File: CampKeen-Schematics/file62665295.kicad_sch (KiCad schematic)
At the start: 29 parts, among them Q2 2N7000, Q3 IRF9Z34NPBF, Q4 2N7000, Q5 2N7000, Q58 LTV-847, Q6 2N7000, Q7 2N7000

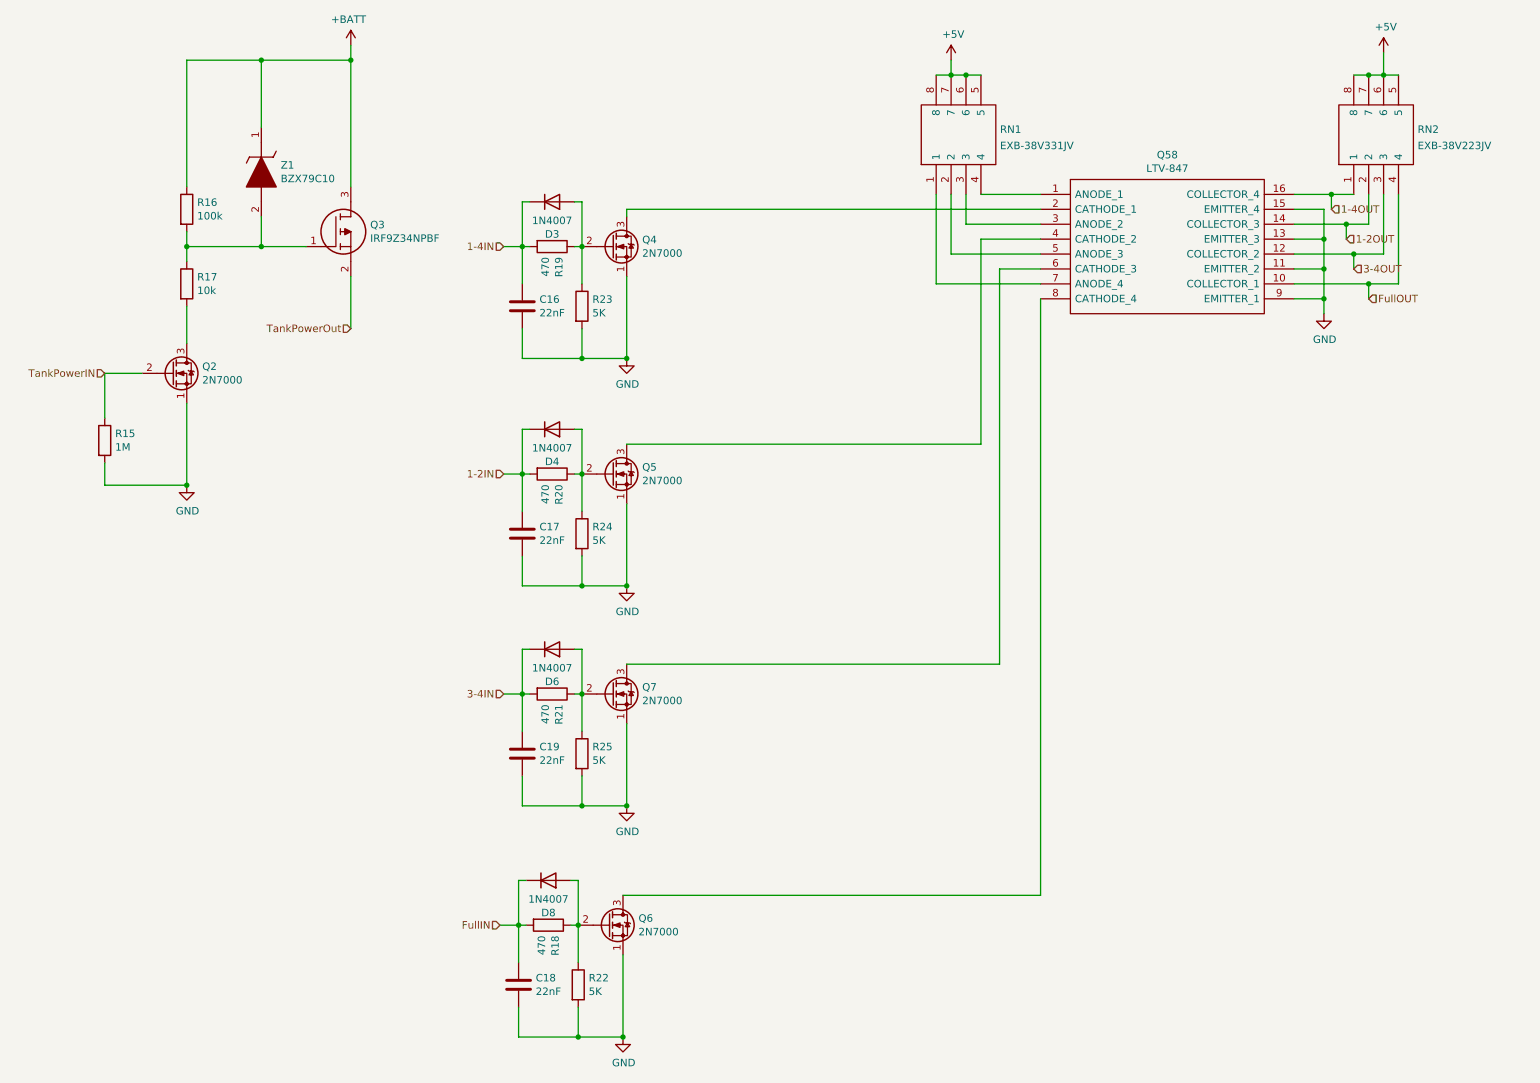
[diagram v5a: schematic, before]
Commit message: working on the input changes. removing all of the inverters. requires a code change. waiting on a part file to add the possible TVS diode
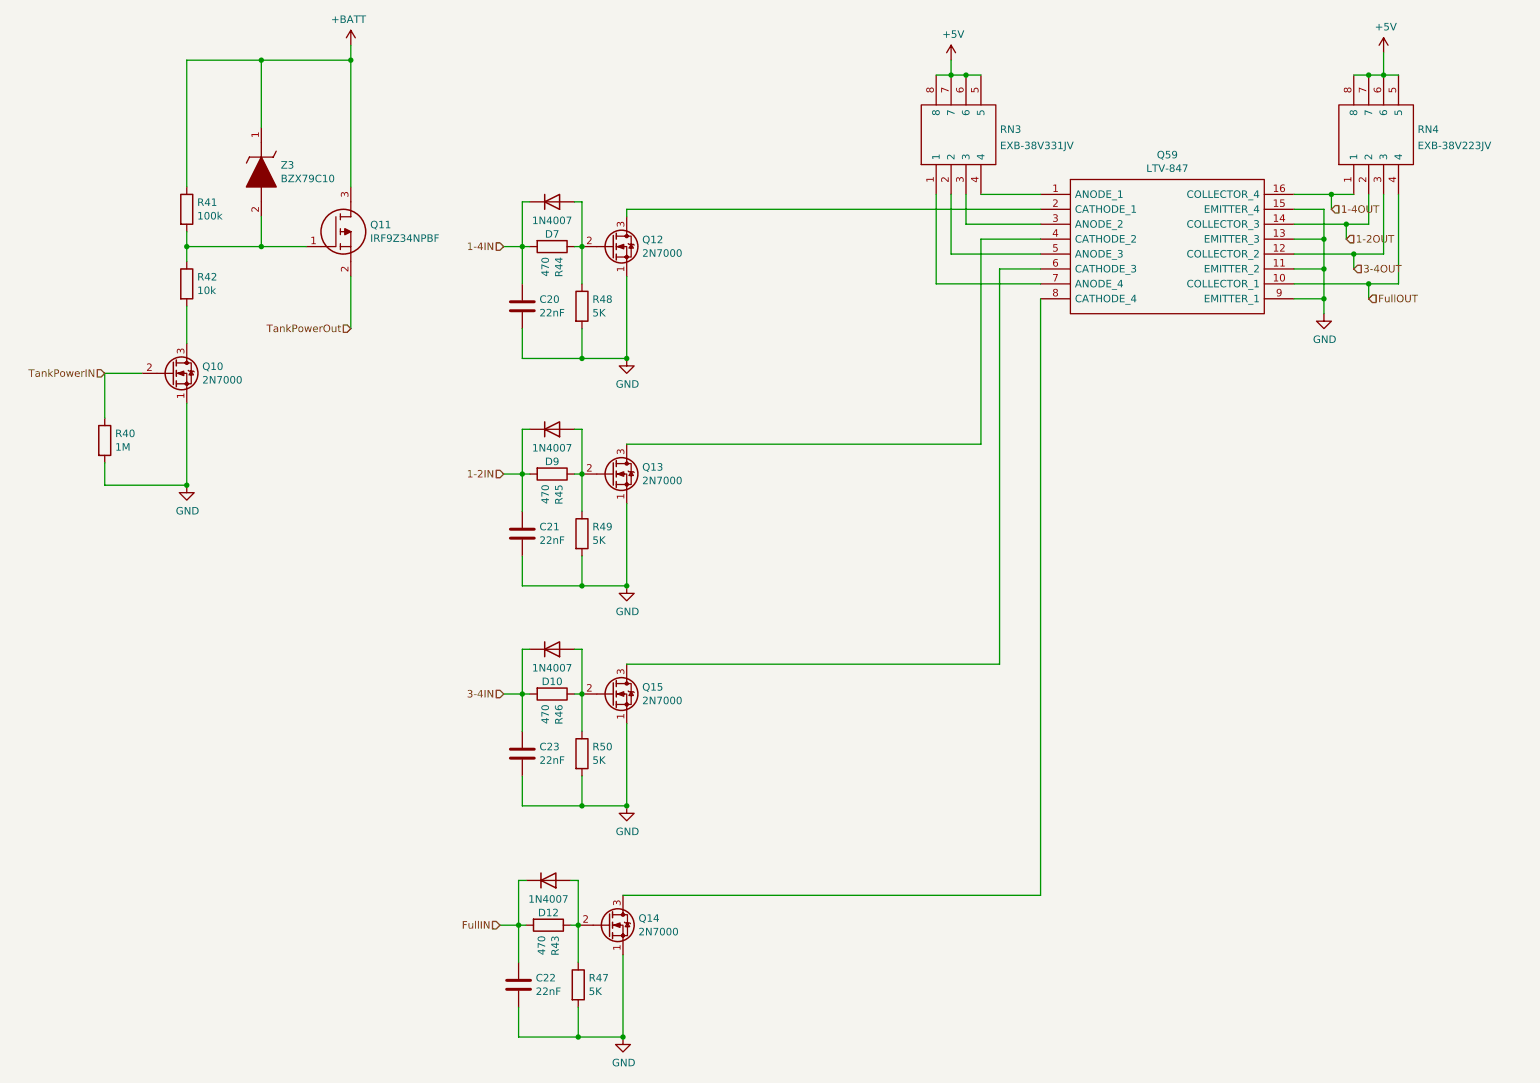
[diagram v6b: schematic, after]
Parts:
- C20: renamed from C16; footprint Capacitor_THT:C_Disc_D4.7mm_W2.5mm_P5.00mm -> Capacitor_SMD:C_0603_1608Metric_Pad1.08x0.95mm_HandSolder
- C21: renamed from C17; footprint Capacitor_THT:C_Disc_D4.7mm_W2.5mm_P5.00mm -> Capacitor_SMD:C_0603_1608Metric_Pad1.08x0.95mm_HandSolder
- C22: renamed from C18; footprint Capacitor_THT:C_Disc_D4.7mm_W2.5mm_P5.00mm -> Capacitor_SMD:C_0603_1608Metric_Pad1.08x0.95mm_HandSolder
- C23: renamed from C19; footprint Capacitor_THT:C_Disc_D4.7mm_W2.5mm_P5.00mm -> Capacitor_SMD:C_0603_1608Metric_Pad1.08x0.95mm_HandSolder
- renumbered D6 to D10, D8 to D12, D3 to D7, D4 to D9, Q2 to Q10, Q3 to Q11, Q4 to Q12, Q5 to Q13, Q6 to Q14, Q7 to Q15, Q58 to Q59, R15 to R40, R16 to R41, R17 to R42, R18 to R43, R19 to R44, R20 to R45, R21 to R46, R22 to R47, R23 to R48, R24 to R49, R25 to R50, RN1 to RN3, RN2 to RN4, Z1 to Z3

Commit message: working on getting the board cleaned enough to start placing the new designs and chips.
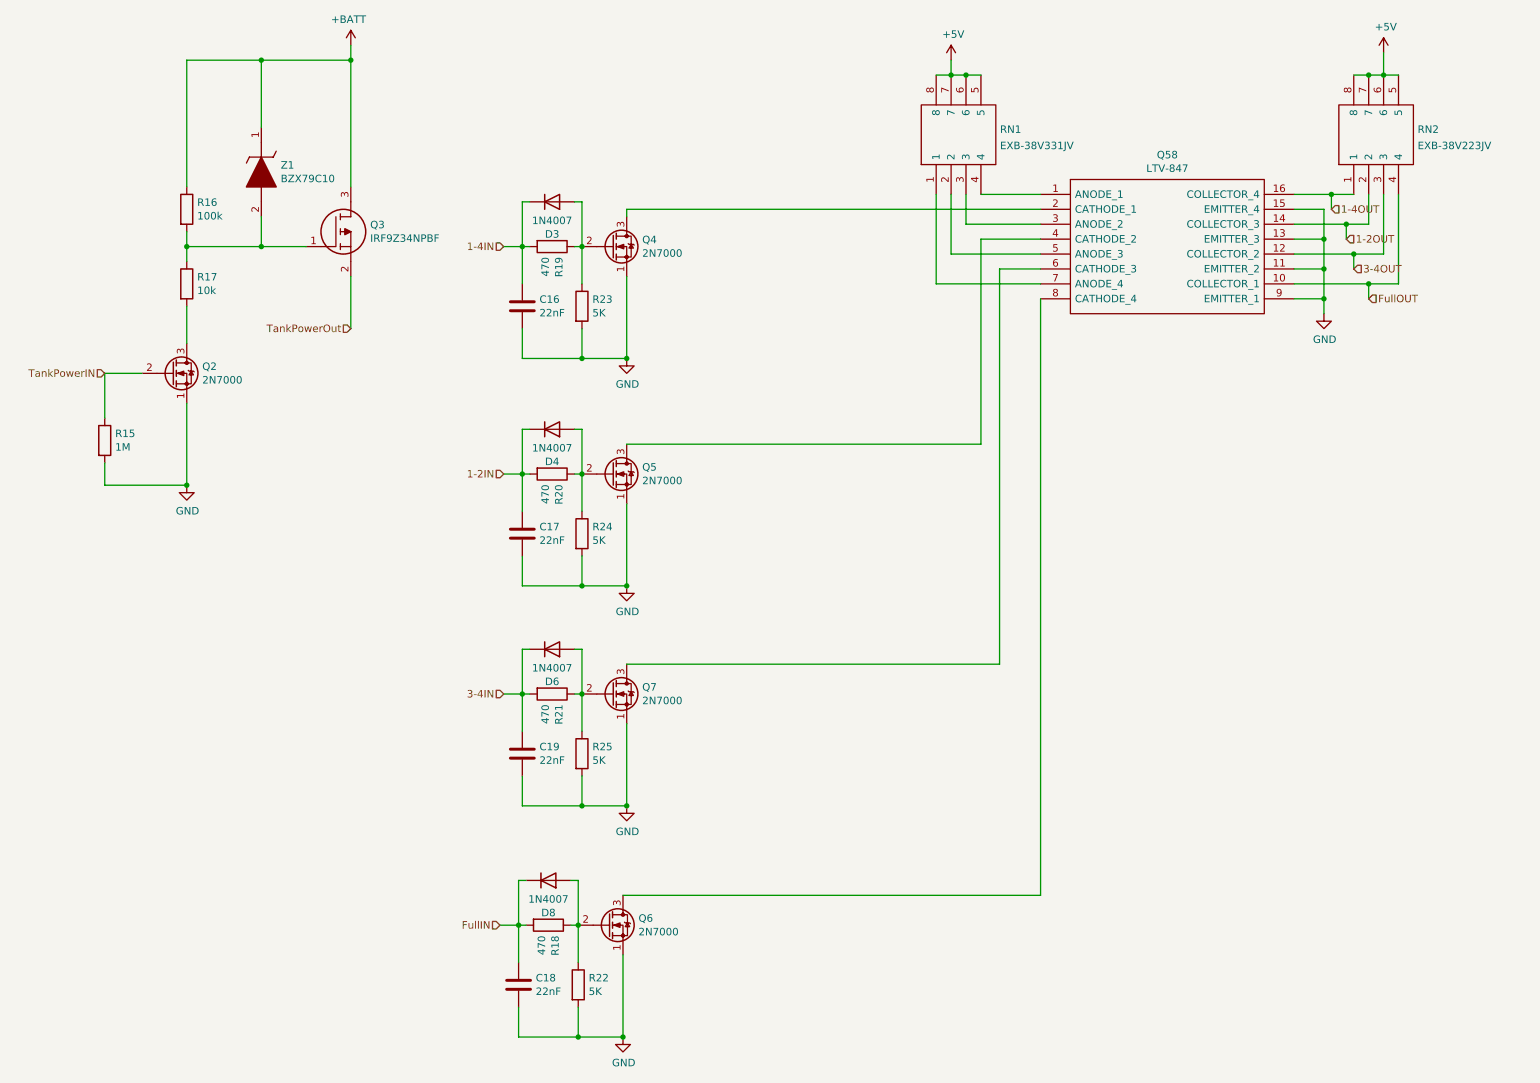
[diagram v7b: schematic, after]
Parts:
- renumbered C20 to C16, C21 to C17, C22 to C18, C23 to C19, D7 to D3, D9 to D4, D10 to D6, D12 to D8, Q10 to Q2, Q11 to Q3, Q12 to Q4, Q13 to Q5, Q59 to Q58, Q14 to Q6, Q15 to Q7, R40 to R15, R41 to R16, R42 to R17, R43 to R18, R44 to R19, R45 to R20, R46 to R21, R47 to R22, R48 to R23, R49 to R24, R50 to R25, RN3 to RN1, RN4 to RN2, Z3 to Z1

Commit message: alright massive changes. some part switches and some reassignments. mostly it's switching out stuff for SMD so that i have more space.
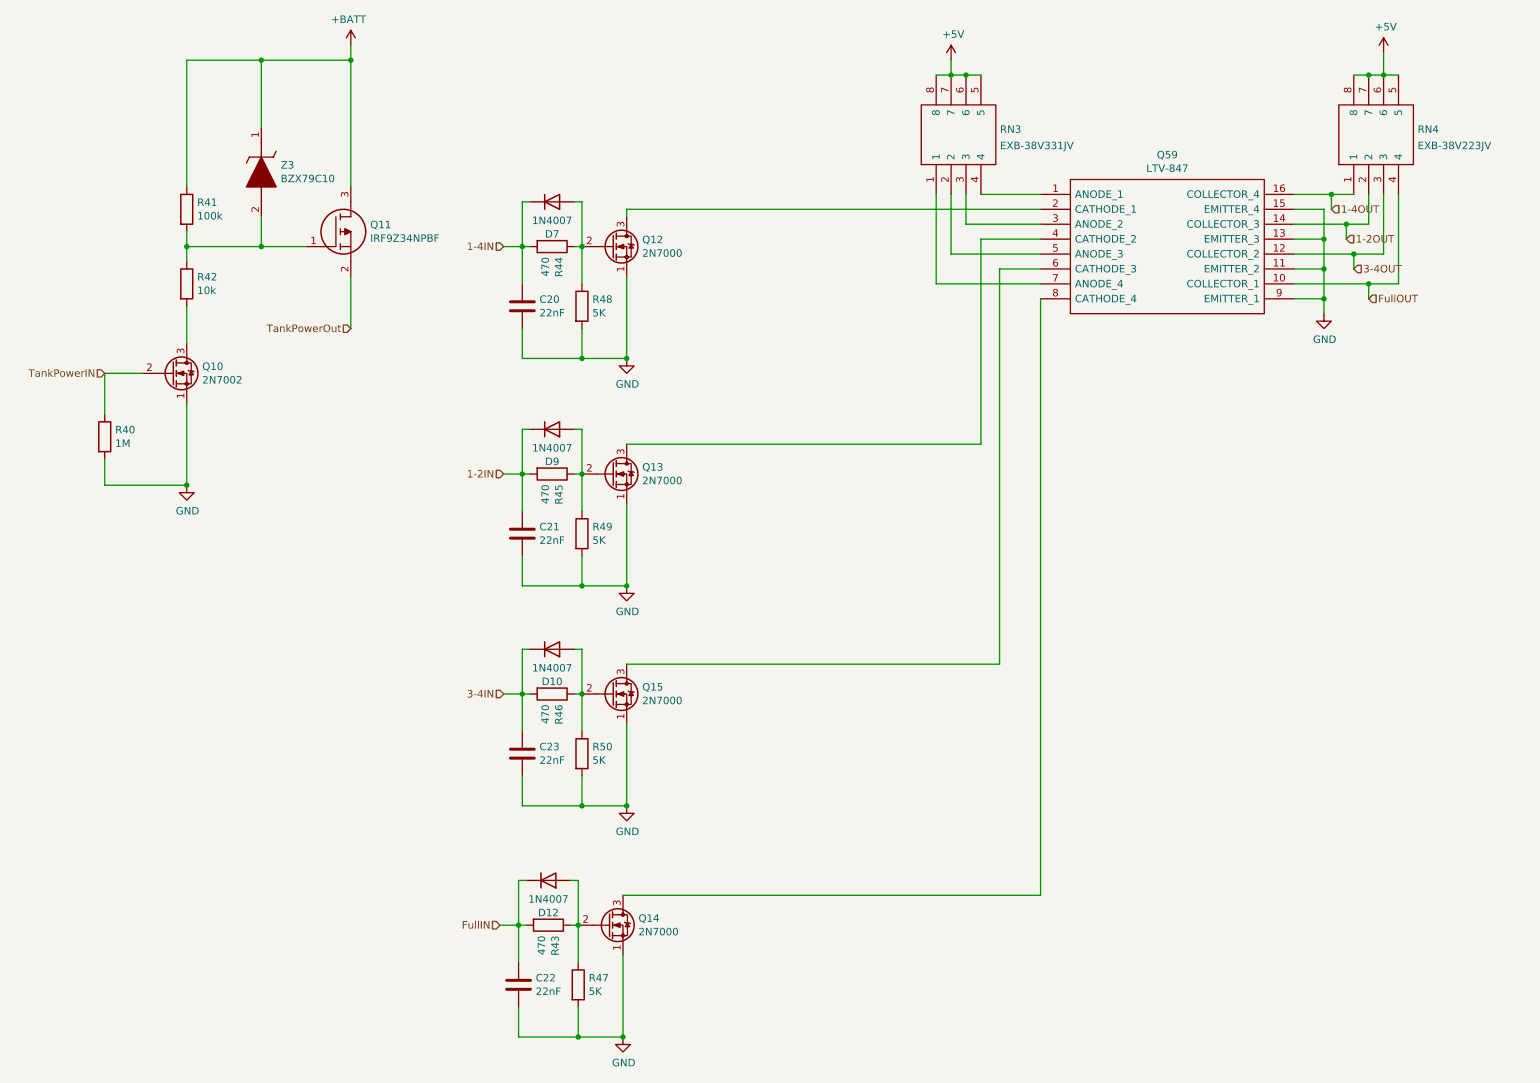
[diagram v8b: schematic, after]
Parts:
- Q10: renamed from Q2; value 2N7000 -> 2N7002; footprint Package_TO_SOT_THT:TO-92_Inline -> Package_TO_SOT_SMD:SOT-23
- renumbered C16 to C20, C17 to C21, C18 to C22, C19 to C23, D6 to D10, D8 to D12, D3 to D7, D4 to D9, Q3 to Q11, Q4 to Q12, Q5 to Q13, Q6 to Q14, Q7 to Q15, Q58 to Q59, R15 to R40, R16 to R41, R17 to R42, R18 to R43, R19 to R44, R20 to R45, R21 to R46, R22 to R47, R23 to R48, R24 to R49, R25 to R50, RN1 to RN3, RN2 to RN4, Z1 to Z3
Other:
- moved on the sheet: R40
